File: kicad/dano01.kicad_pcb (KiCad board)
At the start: 2 copper layers, 257.7 x 98.1 mm, 101 parts, among them J1 1735265-8, J2 1735265-8, J43 Conn_01x03_Pin, SW1 SW_Push, SW10 SW_Push, SW11 SW_Push, SW12 SW_Push, SW13 SW_Push, SW14 SW_Push, SW15 SW_Push, SW16 SW_Push, SW17 SW_Push, SW18 SW_Push, SW19 SW_Push, SW2 SW_Push, SW20 SW_Push, SW21 SW_Push, SW22 SW_Push, SW23 SW_Push, SW24 SW_Push, SW25 SW_Push, SW26 SW_Push, SW27 SW_Push, SW28 SW_Push, SW29 SW_Push, SW3 SW_Push, SW30 SW_Push, SW31 SW_Push, SW32 SW_Push, SW33 SW_Push, SW34 SW_Push, SW35 SW_Push, SW36 SW_Push, SW37 SW_Push, SW38 SW_Push, SW39 SW_Push, SW4 SW_Push, SW40 SW_Push, SW41 SW_Push, SW42 SW_Push, SW43 SW_Push, SW44 SW_Push, SW45 SW_Push, SW46 SW_Push, SW47 SW_Push, SW48 SW_Push, SW5 SW_Push, SW6 SW_Push, SW7 SW_Push, SW8 SW_Push, SW9 SW_Push

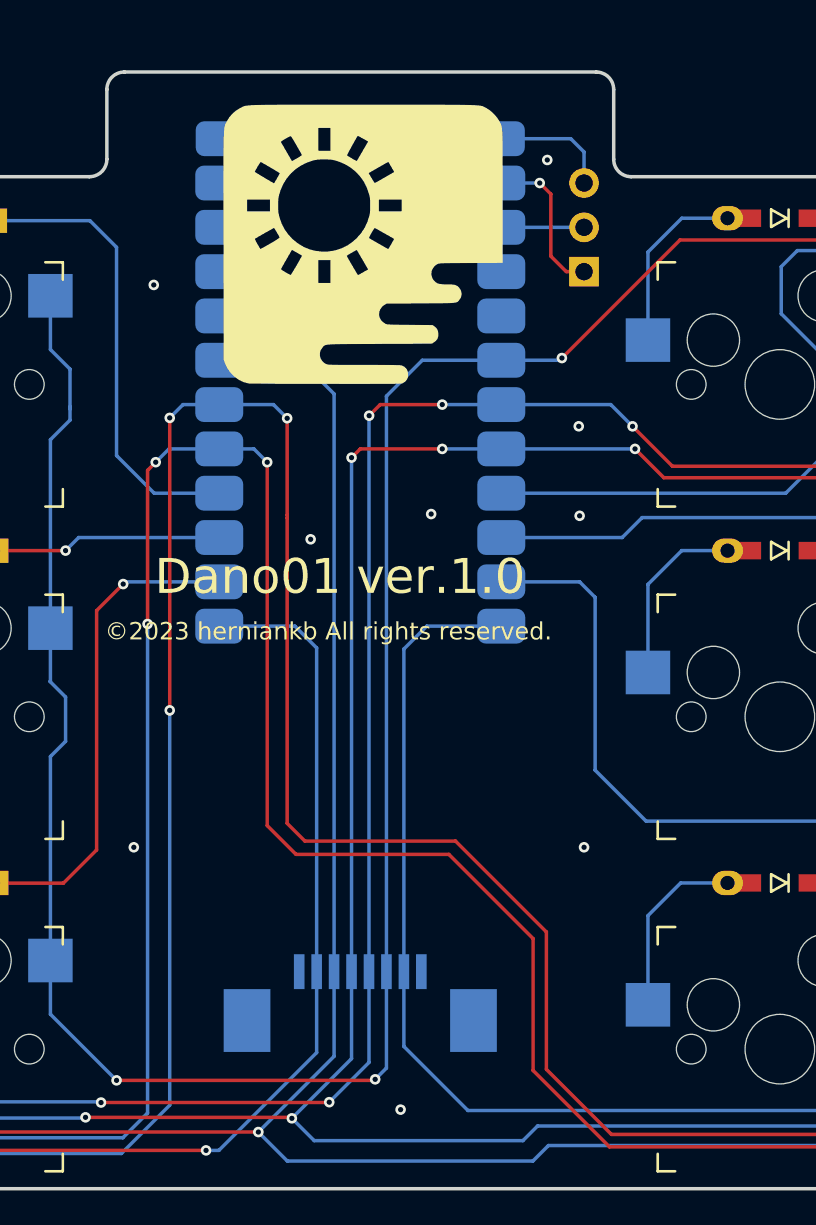
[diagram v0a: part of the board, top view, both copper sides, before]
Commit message: 2012/12/18にFusionPCBへ製造依頼をしたもの
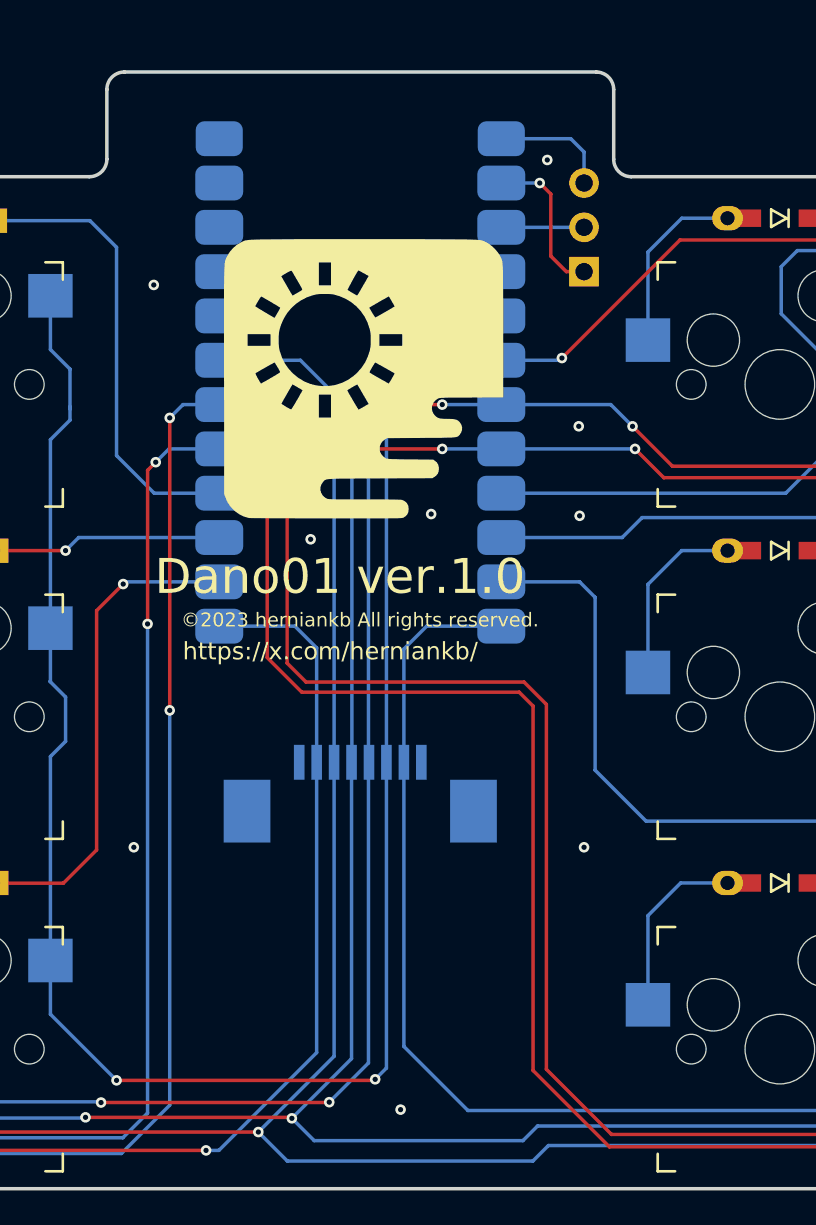
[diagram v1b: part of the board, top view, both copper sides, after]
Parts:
- moved J1 12.0 mm to (148.6, 97.1)
- moved G*** 7.71 mm to (148.8, 71.9)
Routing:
- net col2: track 428.8 -> 431.1 mm
- net col1: track 461.5 -> 463.7 mm
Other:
- board text added: "https://x.com/herniankb/"

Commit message: Ver. 1.1の発注版
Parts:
- added RSW1: SW_Push, kbd:ResetSW_1side, B.Cu at (133.1, 62.8)
- B1: value PRO_MICRO -> SPARKFUN_PRO_MICRO
- D1, D10, D11, D12, D13, D14, D15, D16, D17, D18, D19, D2, D20, D21, D22, D23, D24, D25, D26, D27, D28, D29, D3, D30, D31, D32, D33, D34, D35, D36, D37, D38, D39, D4, D40, D41, D42, D43, D44, D45, D46, D47, D48, D5, D6, D7, D8, D9: moved to B.Cu
- moved D6 2.74 mm to (121.7, 62.8)
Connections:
- B1 pad 22: unconnected-(B1-RESET-Pad22) -> Net-(B1-RESET)
- B1 pad 23: unconnected-(B1-GND-Pad23) -> Net-(B1-GND-Pad23)
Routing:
- net Net-(B1-RESET): track 0.00 -> 12.0 mm
- net Net-(B1-GND-Pad23): track 0.00 -> 5.45 mm
- net col2: track 431.1 -> 425.9 mm
- net col1: track 463.7 -> 459.2 mm
- net Net-(D6-A): track 10.2 -> 7.65 mm
- net col4: track 340.6 -> 339.2 mm
- net col5: track 225.1 -> 223.8 mm
- net row2: track 124.4 -> 123.2 mm
- net row4: track 151.9 -> 151.3 mm
- net row1: track 148.7 -> 148.2 mm
- net GND: vias 35 -> 34
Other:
- board text added: "Dano01 ver.1.1"
- board text removed: "Dano01 ver.1.0"
